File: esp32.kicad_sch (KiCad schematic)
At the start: 19 parts, among them J5 UART, J6 ToSSR, J7 USB_A, Q1 BSS138, SW1 SW_Push, SW2 SW_Push, U1 ESP32-S3-WROOM-1

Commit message: fix: after ERC check
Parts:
- Q1: footprint Package_TO_SOT_SMD:SOT-23-3 -> Package_TO_SOT_SMD:SOT-23
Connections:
- net at J5.2 (Pin_2): now also U1.37 (TXD0)
- net at J5.3 (Pin_3): now also U1.36 (RXD0)
- no-connect marks 3 -> 17
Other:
- moved on the sheet: C14, J5

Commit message: fix: add pull-up resistor to IO0 pin (boot mode)
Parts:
- added R18: 10k, Resistor_THT:R_Axial_DIN0207_L6.3mm_D2.5mm_P7.62mm_Horizontal, symbol Device:R
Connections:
- net +3V3: now also R18.2
- net IO0: now also R18.1
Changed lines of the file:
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@@
-	(wire
-		(pts
-			(xy 66.04 71.12) (xy 77.47 71.12)
-		)
-		(stroke
-			(width 0)
-			(type default)
-		)
-	)
 	(wire
 		(pts
@@
 	(wire
 		(pts
+			(xy 34.29 71.12) (xy 77.47 71.12)
+		)
+		(stroke
+			(width 0)
+			(type default)
+		)
+	)
+	(wire
+		(pts
 			(xy 255.27 127) (xy 236.22 127)
 		)
@@
 	(wire
 		(pts
+			(xy 34.29 57.15) (xy 34.29 50.8)
+		)
+		(stroke
+			(width 0)
+			(type default)
+		)
+	)
+	(wire
+		(pts
 			(xy 133.35 55.88) (xy 133.35 63.5)
 		)
@@
 		(pts
 			(xy 92.71 49.53) (xy 92.71 54.61)
+		)
+		(stroke
+			(width 0)
+			(type default)
+		)
+	)
+	(wire
+		(pts
+			(xy 34.29 64.77) (xy 34.29 71.12)
 		)
 		(stroke
@@
 				(path "/08ef31dc-81c2-4bcd-8336-e62c344e451e/5b2a06a5-fb5f-4aba-bfde-32c85173e89f"
 					(reference "R11")
+					(unit 1)
+				)
+			)
+		)
+	)
+	(symbol
+		(lib_id "Device:R")
+		(at 34.29 60.96 180)
+		(unit 1)
+		(exclude_from_sim no)
+		(in_bom yes)
+		(on_board yes)
+		(dnp no)
+		(property "Reference" "R18"
+			(at 27.94 60.96 90)
+			(effects
+				(font
+					(size 1.27 1.27)
+				)
+			)
+		)
+		(property "Value" "10k"
+			(at 30.48 60.96 90)
+			(effects
+				(font
+					(size 1.27 1.27)
+				)
+			)
+		)
+		(property "Footprint" "Resistor_THT:R_Axial_DIN0207_L6.3mm_D2.5mm_P7.62mm_Horizontal"
+			(at 36.068 60.96 90)
+			(effects
+				(font
+					(size 1.27 1.27)
+				)
+				(hide yes)
+			)
+		)
+		(property "Datasheet" "~"
+			(at 34.29 60.96 0)
+			(effects
+				(font
+					(size 1.27 1.27)
+				)
+				(hide yes)
+			)
+		)
+		(property "Description" "Resistor"
+			(at 34.29 60.96 0)
+			(effects
+				(font
+					(size 1.27 1.27)
+				)
+				(hide yes)
+			)
+		)
+		(pin "2"
+		)
+		(pin "1"
+		)
+		(instances
+			(project "pv_router"
+				(path "/08ef31dc-81c2-4bcd-8336-e62c344e451e/5b2a06a5-fb5f-4aba-bfde-32c85173e89f"
+					(reference "R18")
 					(unit 1)
 				)
@@
 					(unit 1)
 				)
+			)
+		)
+	)
+	(symbol
+		(lib_id "power:+3V3")
+		(at 34.29 50.8 0)
+		(unit 1)
+		(exclude_from_sim no)
+		(in_bom yes)
+		(on_board yes)
+		(dnp no)
+		(fields_autoplaced yes)
+		(property "Reference" "#PWR044"
+			(at 34.29 54.61 0)
+			(effects
+				(font
+					(size 1.27 1.27)
+				)
+				(hide yes)
+			)
+		)
+		(property "Value" "+3V3"
+			(at 34.29 45.72 0)
+			(effects
+				(font
+					(size 1.27 1.27)
+				)
+			)
+		)
+		(property "Footprint" ""
+			(at 34.29 50.8 0)
+			(effects
+				(font
+					(size 1.27 1.27)
+				)
+				(hide yes)
+			)
+		)
+		(property "Datasheet" ""
+			(at 34.29 50.8 0)
+			(effects
+				(font
+					(size 1.27 1.27)
+				)
+				(hide yes)
+			)
+		)
+		(property "Description" "Power symbol creates a global label with name \"+3V3\""
+			(at 34.29 50.8 0)
+			(effects
+				(font
+					(size 1.27 1.27)
+				)
+				(hide yes)
+			)
+		)
+		(pin "1"
+		)
+		(instances
+			(project "pv_router"
+				(path "/08ef31dc-81c2-4bcd-8336-e62c344e451e/5b2a06a5-fb5f-4aba-bfde-32c85173e89f"
+					(reference "#PWR044")
+					(unit 1)
+				)

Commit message: fix: fix components footprints, resistors, crystal
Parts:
- D5: footprint UET14A05L03BK -> UET14A05L03-BK:UET14A05L03BK
- J6: footprint (none) -> Connector_JST:JST_XH_S2B-XH-A_1x02_P2.50mm_Horizontal
- J7: footprint (none) -> Connector_USB:USB_A_Molex_67643_Horizontal
- R11, R18: footprint Resistor_THT:R_Axial_DIN0207_L6.3mm_D2.5mm_P7.62mm_Horizontal -> Resistor_SMD:R_0805_2012Metric_Pad1.20x1.40mm_HandSolder
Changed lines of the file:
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@@
 			)
 		)
-		(property "Footprint" "Resistor_THT:R_Axial_DIN0207_L6.3mm_D2.5mm_P7.62mm_Horizontal"
+		(property "Footprint" "Resistor_SMD:R_0805_2012Metric_Pad1.20x1.40mm_HandSolder"
 			(at 77.47 39.878 90)
 			(effects
@@
 			)
 		)
-		(property "Footprint" "Resistor_THT:R_Axial_DIN0207_L6.3mm_D2.5mm_P7.62mm_Horizontal"
+		(property "Footprint" "Resistor_SMD:R_0805_2012Metric_Pad1.20x1.40mm_HandSolder"
 			(at 36.068 60.96 90)
 			(effects
@@
 			)
 		)
-		(property "Footprint" ""
+		(property "Footprint" "Connector_USB:USB_A_Molex_67643_Horizontal"
 			(at 240.03 85.09 0)
 			(effects
@@
 			)
 		)
-		(property "Footprint" ""
+		(property "Footprint" "Connector_JST:JST_XH_S2B-XH-A_1x02_P2.50mm_Horizontal"
 			(at 196.85 69.85 0)
 			(effects
@@
 			)
 		)
-		(property "Footprint" "UET14A05L03BK"
+		(property "Footprint" "UET14A05L03-BK:UET14A05L03BK"
 			(at 350.19 99.06 0)
 			(effects

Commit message: fix: FP for USB connector and schotky diode
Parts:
- J7: footprint Connector_USB:USB_A_Molex_67643_Horizontal -> USB_A_61400416021:USB-2.0-TYPE-A
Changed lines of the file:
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@@
 			)
 		)
-		(property "Footprint" "Connector_USB:USB_A_Molex_67643_Horizontal"
+		(property "Footprint" "USB_A_61400416021:USB-2.0-TYPE-A"
 			(at 240.03 85.09 0)
 			(effects

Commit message: fix: update SMD FP components to handsoldering
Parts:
- C15: footprint Capacitor_SMD:C_0805_2012Metric_Pad1.18x1.45mm_HandSolder -> Capacitor_SMD:C_1210_3225Metric_Pad1.33x2.70mm_HandSolder
- Q1: footprint Package_TO_SOT_SMD:SOT-23 -> Package_TO_SOT_SMD:SOT-23_Handsoldering
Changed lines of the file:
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@@
 			)
 		)
-		(property "Footprint" "Capacitor_SMD:C_0805_2012Metric_Pad1.18x1.45mm_HandSolder"
+		(property "Footprint" "Capacitor_SMD:C_1210_3225Metric_Pad1.33x2.70mm_HandSolder"
 			(at 92.71 48.5648 0)
 			(effects
@@
 			)
 		)
-		(property "Footprint" "Package_TO_SOT_SMD:SOT-23"
+		(property "Footprint" "Package_TO_SOT_SMD:SOT-23_Handsoldering"
 			(at 186.69 93.345 0)
 			(effects

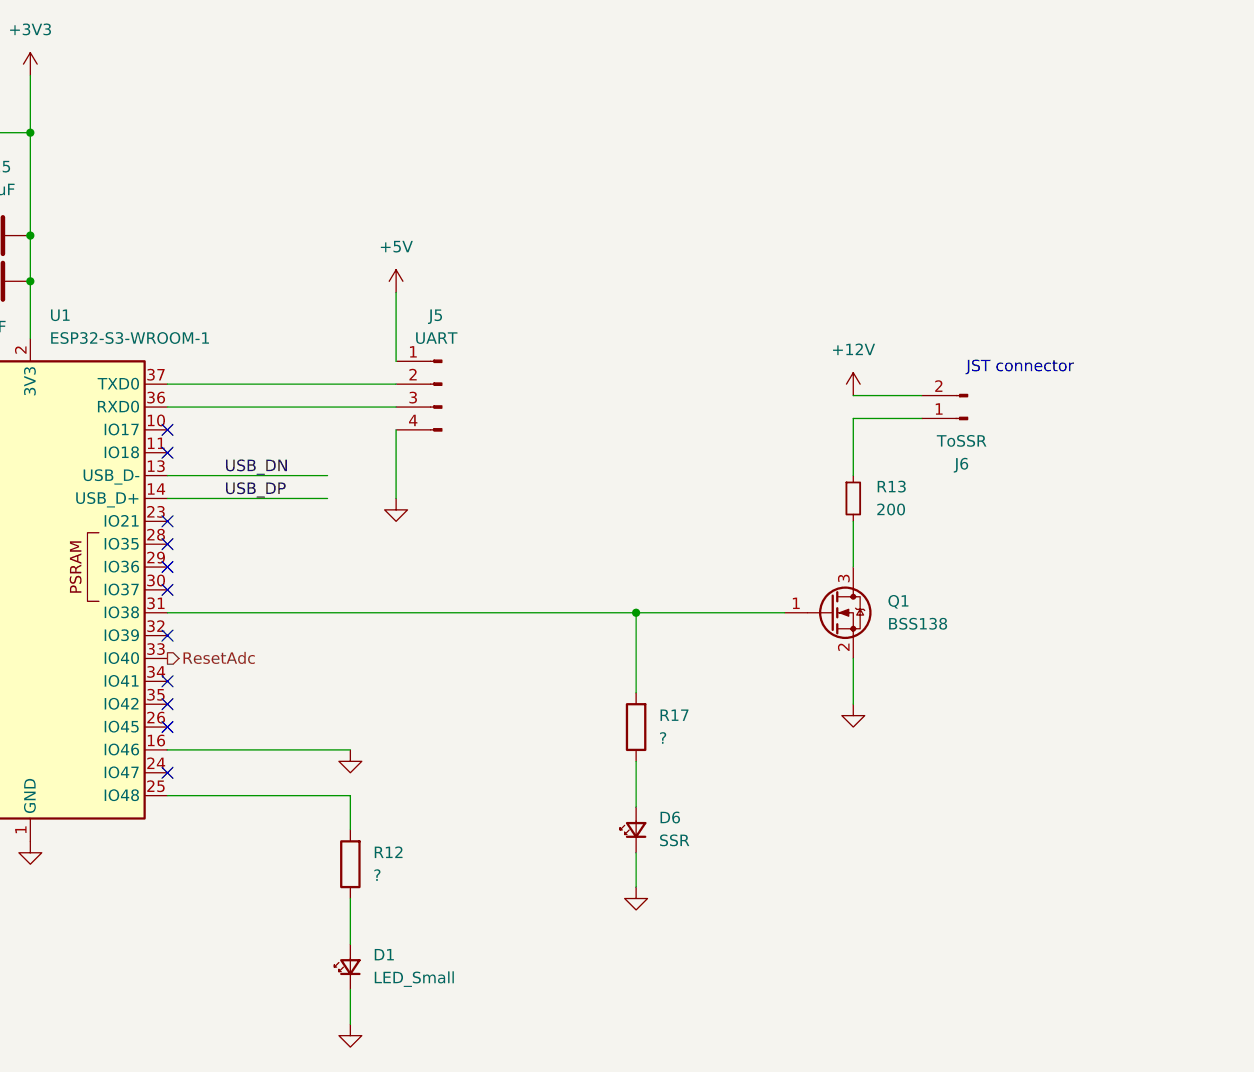
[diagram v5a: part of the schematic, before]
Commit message: fix: reconnect SSR FET to ESP32
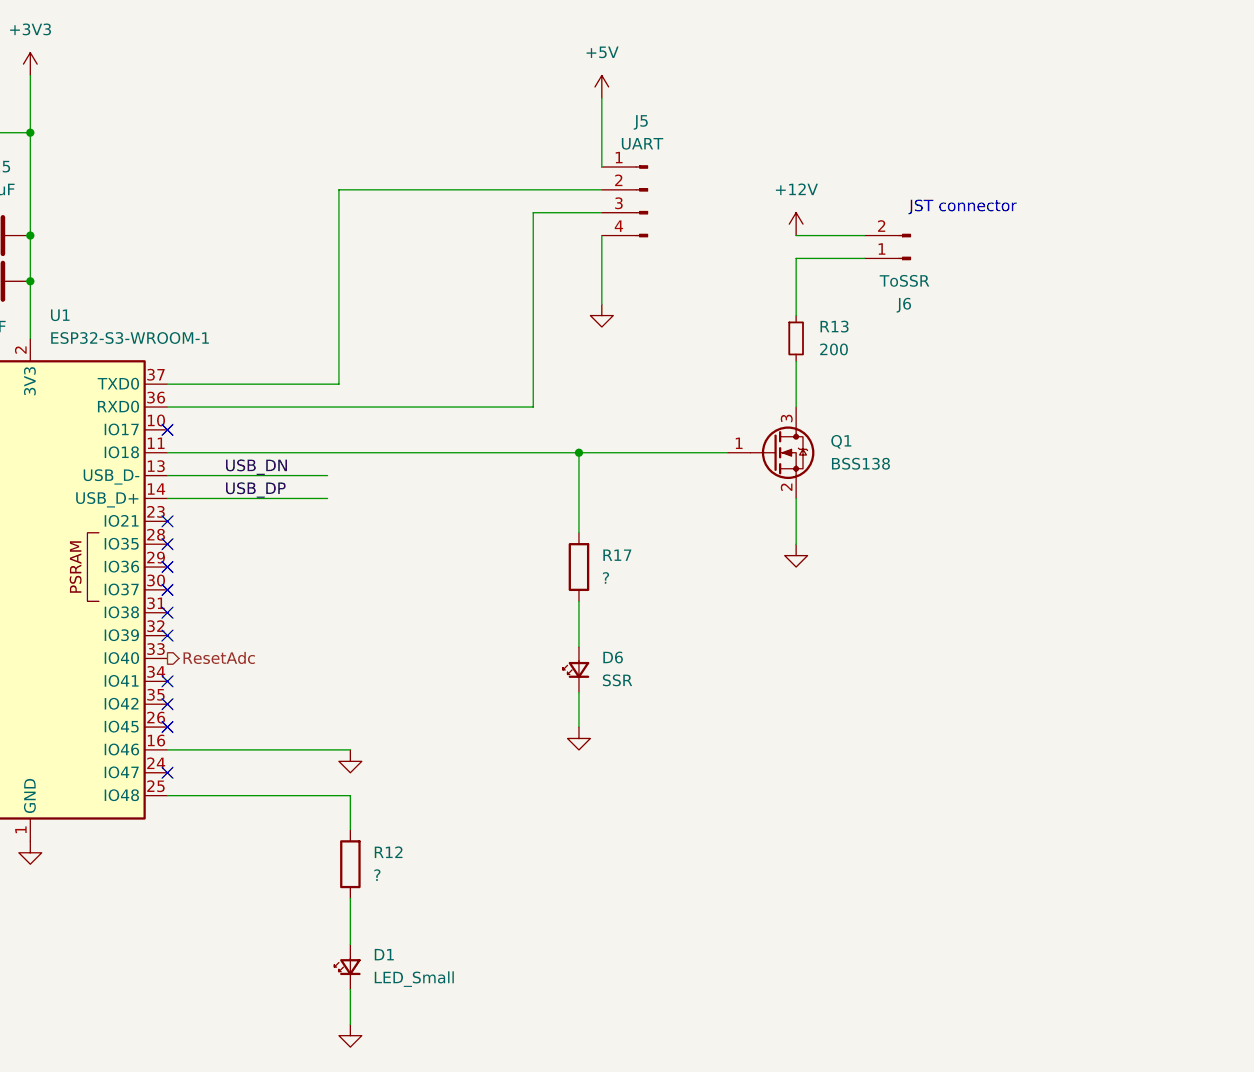
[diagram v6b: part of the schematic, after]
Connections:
- net at U1.11 (IO18): now also Q1.1 (G), R17.2
- now unconnected: U1.31 (IO38)
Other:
- moved on the sheet: D6, J5, J6, Q1, R13, R17

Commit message: feat: add test points
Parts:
- added TP2, TP3, TP5: TestPoint, TestPoint:TestPoint_THTPad_D1.5mm_Drill0.7mm, symbol Connector:TestPoint
- added TP4: TestPoint, TestPoint:TestPoint_Pad_D2.0mm, symbol Connector:TestPoint
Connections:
- net +5V: now also TP4.1
- net USB_DN: now also TP3.1
- net USB_DP: now also TP2.1
- net at J6.1 (Pin_1), R13.1: now also TP5.1

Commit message: feat: tracking OK
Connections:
- net CF1: now also U1.25 (IO48); no longer U1.4 (IO4)
- net CF2: now also U1.24 (IO47); no longer U1.5 (IO5)
- net IRQ: now also U1.23 (IO21); no longer U1.6 (IO6)
- net WarnIn: now also U1.26 (IO45); no longer U1.7 (IO7)
- net at R12.2: now also U1.31 (IO38); no longer U1.25 (IO48)
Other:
- moved on the sheet: D1, R12
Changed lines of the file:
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@@
 	)
 	(no_connect
-		(at 107.95 81.28)
+		(at 77.47 76.2)
 	)
 	(no_connect
-		(at 107.95 109.22)
+		(at 77.47 93.98)
 	)
 	(no_connect
-		(at 77.47 76.2)
+		(at 77.47 86.36)
 	)
 	(no_connect
-		(at 77.47 93.98)
+		(at 77.47 83.82)
 	)
 	(no_connect
@@
 	)
 	(no_connect
-		(at 107.95 91.44)
+		(at 107.95 93.98)
 	)
 	(no_connect
-		(at 107.95 93.98)
+		(at 77.47 81.28)
 	)
 	(no_connect
@@
 	)
 	(no_connect
-		(at 107.95 83.82)
+		(at 77.47 88.9)
 	)
 	(no_connect
-		(at 107.95 104.14)
+		(at 107.95 83.82)
 	)
 	(wire
@@
 	(wire
 		(pts
-			(xy 128.27 133.35) (xy 128.27 137.16)
+			(xy 142.24 114.3) (xy 142.24 118.11)
 		)
 		(stroke
@@
 	(wire
 		(pts
-			(xy 128.27 111.76) (xy 128.27 115.57)
+			(xy 142.24 91.44) (xy 142.24 96.52)
 		)
 		(stroke
@@
 	(wire
 		(pts
-			(xy 128.27 123.19) (xy 128.27 128.27)
+			(xy 142.24 104.14) (xy 142.24 109.22)
 		)
 		(stroke
@@
 	(wire
 		(pts
+			(xy 107.95 91.44) (xy 142.24 91.44)
+		)
+		(stroke
+			(width 0)
+			(type default)
+		)
+	)
+	(wire
+		(pts
 			(xy 127 66.04) (xy 107.95 66.04)
 		)
@@
 	(wire
 		(pts
-			(xy 107.95 111.76) (xy 128.27 111.76)
-		)
-		(stroke
-			(width 0)
-			(type default)
-		)
-	)
-	(wire
-		(pts
 			(xy 255.27 125.73) (xy 255.27 127)
 		)
@@
 	(hierarchical_label "CF1"
 		(shape input)
-		(at 77.47 81.28 180)
+		(at 107.95 111.76 0)
 		(effects
 			(font
 				(size 1.27 1.27)
 			)
-			(justify right)
+			(justify left)
 		)
 	)
@@
 	(hierarchical_label "CF2"
 		(shape input)
-		(at 77.47 83.82 180)
+		(at 107.95 109.22 0)
 		(effects
 			(font
 				(size 1.27 1.27)
 			)
-			(justify right)
+			(justify left)
 		)
 	)
 	(hierarchical_label "WarnIn"
 		(shape input)
-		(at 77.47 88.9 180)
+		(at 107.95 104.14 0)
 		(effects
 			(font
 				(size 1.27 1.27)
 			)
-			(justify right)
+			(justify left)
 		)
 	)
 	(hierarchical_label "IRQ"
 		(shape input)
-		(at 77.47 86.36 180)
+		(at 107.95 81.28 0)
 		(effects
 			(font
 				(size 1.27 1.27)
 			)
-			(justify right)
+			(justify left)
 		)
 	)
@@
 	(symbol
 		(lib_id "Device:R")
-		(at 128.27 119.38 180)
+		(at 142.24 100.33 180)
 		(unit 1)
 		(exclude_from_sim no)
@@
 		(fields_autoplaced yes)
 		(property "Reference" "R12"
-			(at 130.81 118.11 0)
+			(at 144.78 99.06 0)
 			(effects
 				(font
@@
 		)
 		(property "Value" "?"
-			(at 130.81 120.65 0)
+			(at 144.78 101.6 0)
 			(effects
 				(font
@@
 		)
 		(property "Footprint" "Resistor_THT:R_Axial_DIN0207_L6.3mm_D2.5mm_P7.62mm_Horizontal"
-			(at 130.048 119.38 90)
+			(at 144.018 100.33 90)
 			(effects
 				(font
@@
 		)
 		(property "Datasheet" "~"
-			(at 128.27 119.38 0)
+			(at 142.24 100.33 0)
 			(effects
 				(font
@@
 		)
 		(property "Description" "Resistor"
-			(at 128.27 119.38 0)
+			(at 142.24 100.33 0)
 			(effects
 				(font
@@
 	(symbol
 		(lib_id "power:GND")
-		(at 128.27 137.16 0)
+		(at 142.24 118.11 0)
 		(unit 1)
 		(exclude_from_sim no)
@@
 		(fields_autoplaced yes)
 		(property "Reference" "#PWR031"
-			(at 128.27 143.51 0)
+			(at 142.24 124.46 0)
 			(effects
 				(font
@@
 		)
 		(property "Value" "GND"
-			(at 128.27 142.24 0)
+			(at 142.24 123.19 0)
 			(effects
 				(font
@@
 		)
 		(property "Footprint" ""
-			(at 128.27 137.16 0)
+			(at 142.24 118.11 0)
 			(effects
 				(font
@@
 		)
 		(property "Datasheet" ""
-			(at 128.27 137.16 0)
+			(at 142.24 118.11 0)
 			(effects
 				(font
@@
 		)
 		(property "Description" "Power symbol creates a global label with name \"GND\" , ground"
-			(at 128.27 137.16 0)
+			(at 142.24 118.11 0)
 			(effects
 				(font
@@
 	(symbol
 		(lib_id "Device:LED_Small")
-		(at 128.27 130.81 90)
+		(at 142.24 111.76 90)
 		(unit 1)
 		(exclude_from_sim no)
@@
 		(fields_autoplaced yes)
 		(property "Reference" "D1"
-			(at 130.81 129.4765 90)
+			(at 144.78 110.4265 90)
 			(effects
 				(font
@@
 		)
 		(property "Value" "LED_Small"
-			(at 130.81 132.0165 90)
+			(at 144.78 112.9665 90)
 			(effects
 				(font
@@
 		)
 		(property "Footprint" "LED_SMD:LED_0805_2012Metric"
-			(at 128.27 130.81 90)
+			(at 142.24 111.76 90)
 			(effects
 				(font
@@
 		)
 		(property "Datasheet" "~"
-			(at 128.27 130.81 90)
+			(at 142.24 111.76 90)
 			(effects
 				(font
@@
 		)
 		(property "Description" "Light emitting diode, small symbol"
-			(at 128.27 130.81 0)
+			(at 142.24 111.76 0)
 			(effects
 				(font
@@
 		)
 		(property "Sim.Pin" "1=K 2=A"
-			(at 128.27 130.81 0)
+			(at 142.24 111.76 0)
 			(effects
 				(font
